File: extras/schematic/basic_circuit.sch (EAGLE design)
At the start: 15 parts, among them M1 ARDUINO-PRO-MINI-3.3V, U1 SI4703

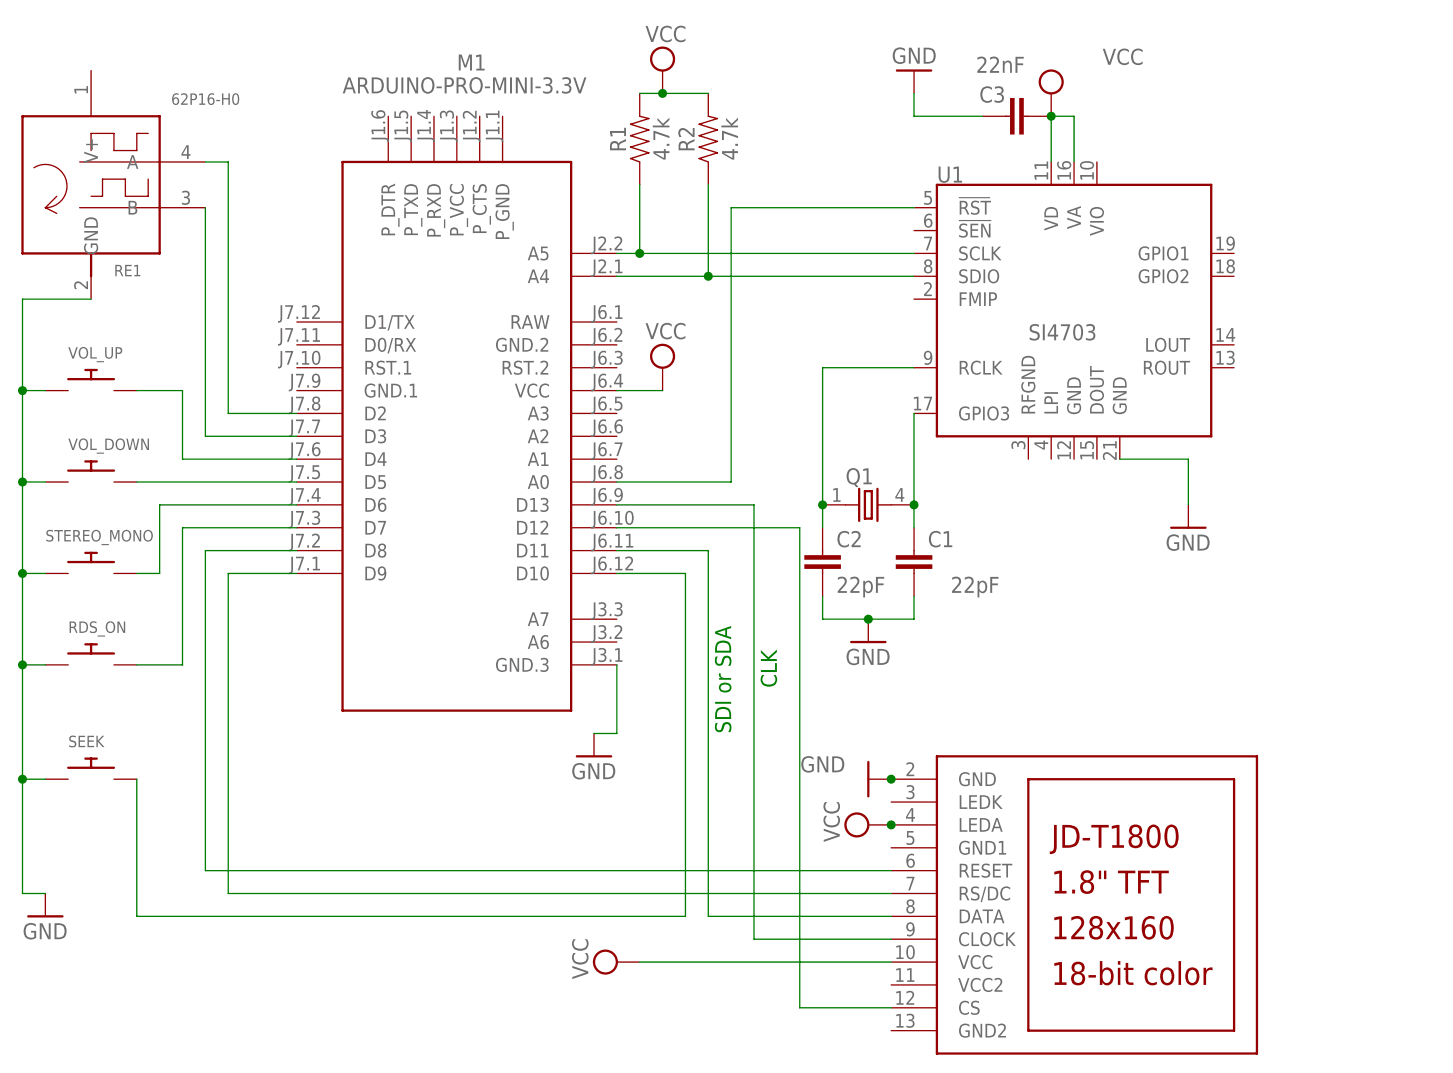
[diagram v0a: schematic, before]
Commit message: SI470X Arduino Library
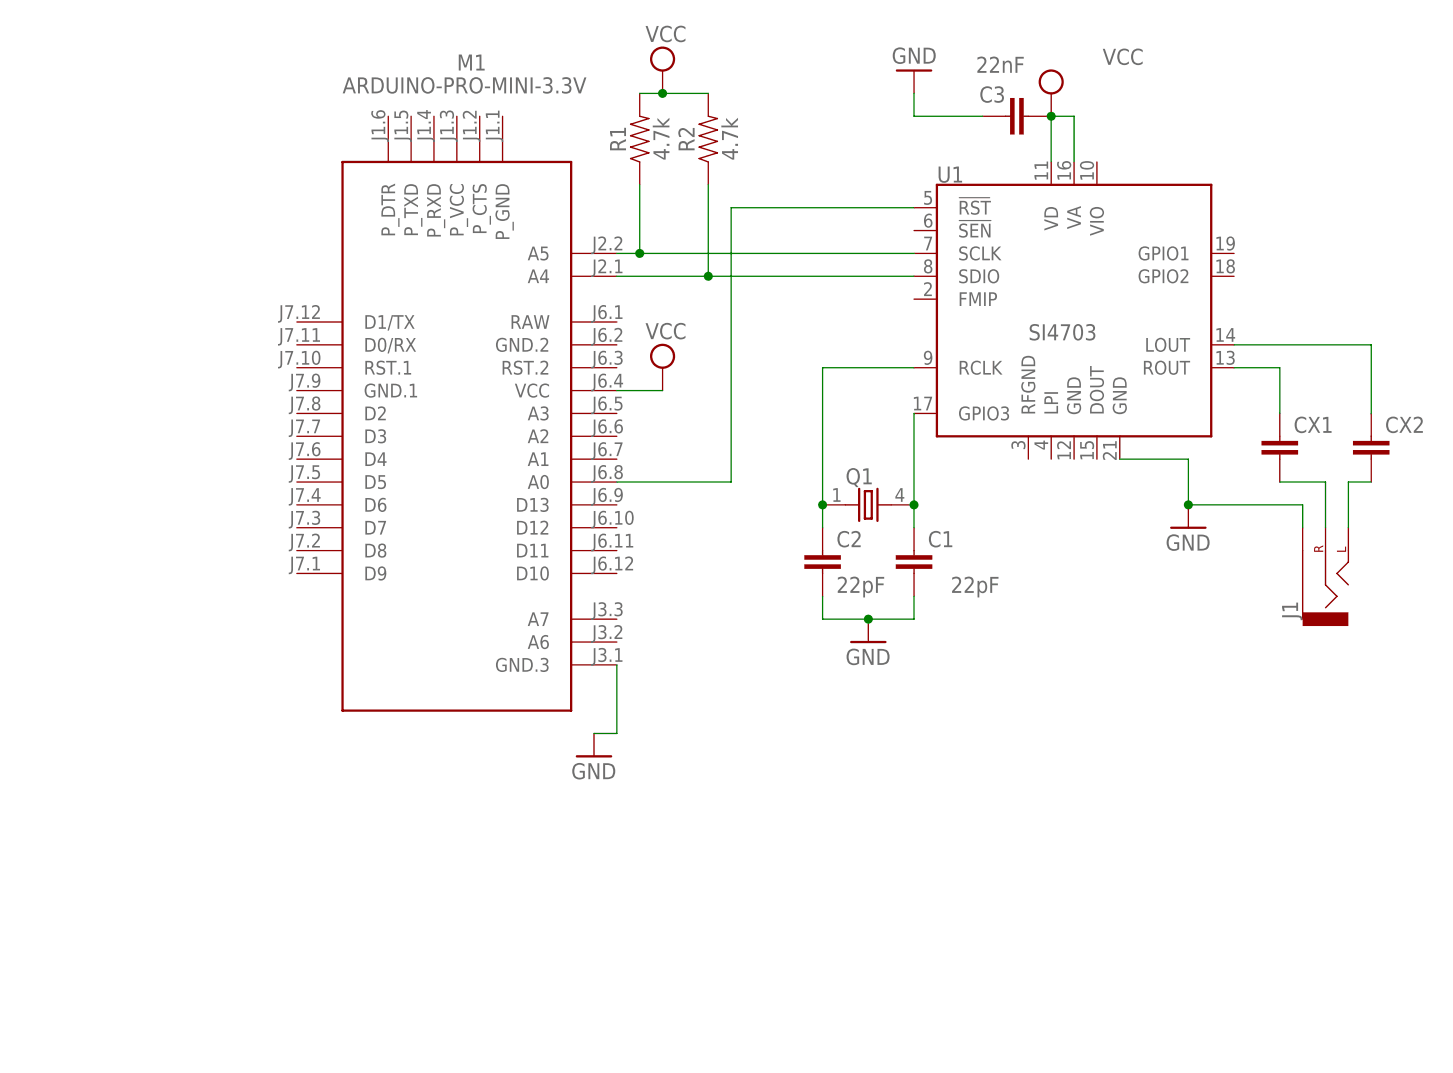
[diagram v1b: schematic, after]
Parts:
- removed LCD1: JD-T1800, adafruit:JD-T1800
- removed RDS_ON, SEEK, STEREO_MONO, VOL_DOWN, VOL_UP: (no value), adafruit:SWITCH_PUSHBUTTONC&K_KSS
- removed RE1: 62P16-H0, rotary-encoder:62P16-H0
- added CX1, CX2: (no value), rcl:CXXC10B6
- added J1: (no value), SparkFun-Connectors:AUDIO_JACK_2.5MM_HOLESONLY
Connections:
- removed net N$10: M1.D6, STEREO_MONO.P$2
- removed net N$11: M1.D7, RDS_ON.P$2
- removed net N$12: LCD1.RESET, M1.D8
- removed net N$13: LCD1.RS/DC, M1.D9
- removed net N$14: LCD1.DATA, M1.D11
- removed net N$15: LCD1.CLOCK, M1.D13
- removed net N$17: M1.D10, SEEK.P$2
- removed net N$18: LCD1.CS, M1.D12
- removed net N$6: M1.D3, RE1.B
- removed net N$7: M1.D2, RE1.A
- removed net N$8: M1.D4, VOL_UP.P$2
- removed net N$9: M1.D5, VOL_DOWN.P$2
- new net N$16: CX1.1, U1.ROUT
- new net N$19: CX2.1, U1.LOUT
- new net N$20: CX1.2, J1.RIGHT
- new net N$21: CX2.2, J1.LEFT
- net GND: now also J1.SLEEVE; no longer LCD1.GND, RDS_ON.P$1, RE1.GND, SEEK.P$1, STEREO_MONO.P$1, VOL_DOWN.P$1, VOL_UP.P$1
- net VCC: no longer LCD1.LEDA, LCD1.VCC
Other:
- note removed: "CLK"
- note removed: "SDI or SDA"
